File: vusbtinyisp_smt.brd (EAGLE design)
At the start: 21 x 29.2 mm, 9 parts, among them J1 AVR_SPI_PRG_6NS, U1 Tiny85-20-SMT

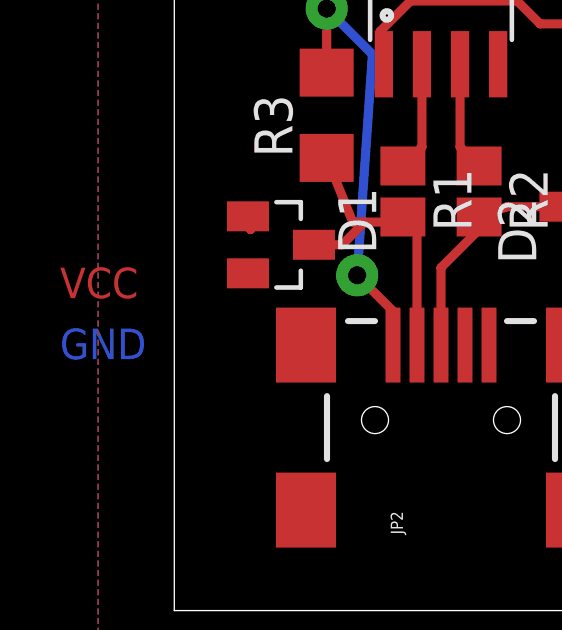
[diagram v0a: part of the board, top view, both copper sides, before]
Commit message: changing 1k to 1.5k resistors in 5V designs
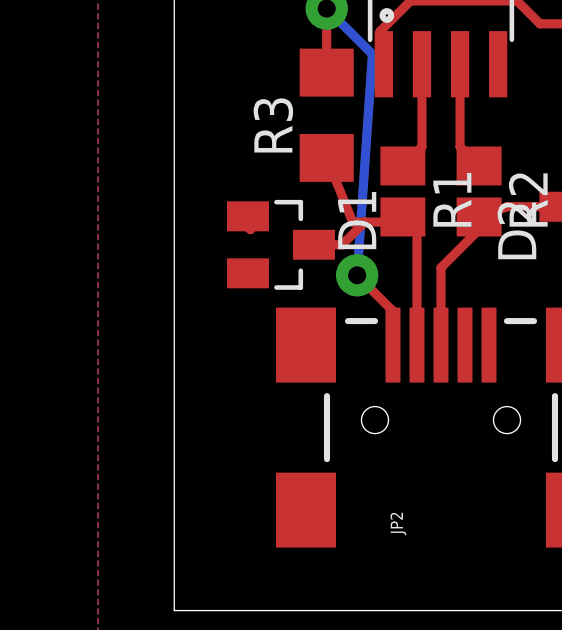
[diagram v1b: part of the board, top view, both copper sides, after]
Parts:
- R3: value 1k Ohm -> 1.5k Ohm
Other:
- board text removed: "GND"
- board text removed: "VCC"
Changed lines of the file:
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@@
 <wire x1="65.456" y1="50.79" x2="44.45" y2="50.79" width="0" layer="20"/>
 <wire x1="44.45" y1="50.79" x2="44.45" y2="21.59" width="0" layer="20"/>
-<text x="40.64" y="32.512" size="1.016" layer="1" align="center-left">VCC</text>
-<text x="40.64" y="30.48" size="1.016" layer="16" align="center-left">GND</text>
 </plain>
 <attributes>
@@
 <element name="R1" library="resistor" package="R0805" value="68ohm" x="52.07" y="35.56" rot="R270"/>
 <element name="R2" library="resistor" package="R0805" value="68 ohm" x="54.61" y="35.56" rot="R270"/>
-<element name="R3" library="resistor" package="R1206" value="1k Ohm" x="49.53" y="38.1" rot="R90"/>
+<element name="R3" library="resistor" package="R1206" value="1.5k Ohm" x="49.53" y="38.1" rot="R90"/>
 <element name="J1" library="SparkFun-Connectors" package="2X3-NS" value="AVR_SPI_PRG_6NS" x="59.944" y="43.688" rot="R270"/>
 <element name="JP2" library="SparkFun-Connectors" package="USB-MINIB" value="USBSMD" x="53.34" y="27.94" rot="R90">
